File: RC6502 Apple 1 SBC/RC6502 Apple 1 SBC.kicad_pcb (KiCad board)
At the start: 2 copper layers, 99.1 x 99.7 mm, 48 parts, among them J1 VP GND, J10 RAM_EN, J11 PIA_EN, J2 Arduino Nano, J3 Backplane, J4 Hole, J5 Hole, J6 Hole, J7 Hole, J8 Power, J9 ROM_EN, SW1 RESET, U1 WD65C02, U2 HM62256BLP-7, U3 74HCT138, U4 28C256, U5 74HCT00, U6 NE555, U7 74HCT04, U8 WD65C21, U9 MCP23S17, X1 1MHz

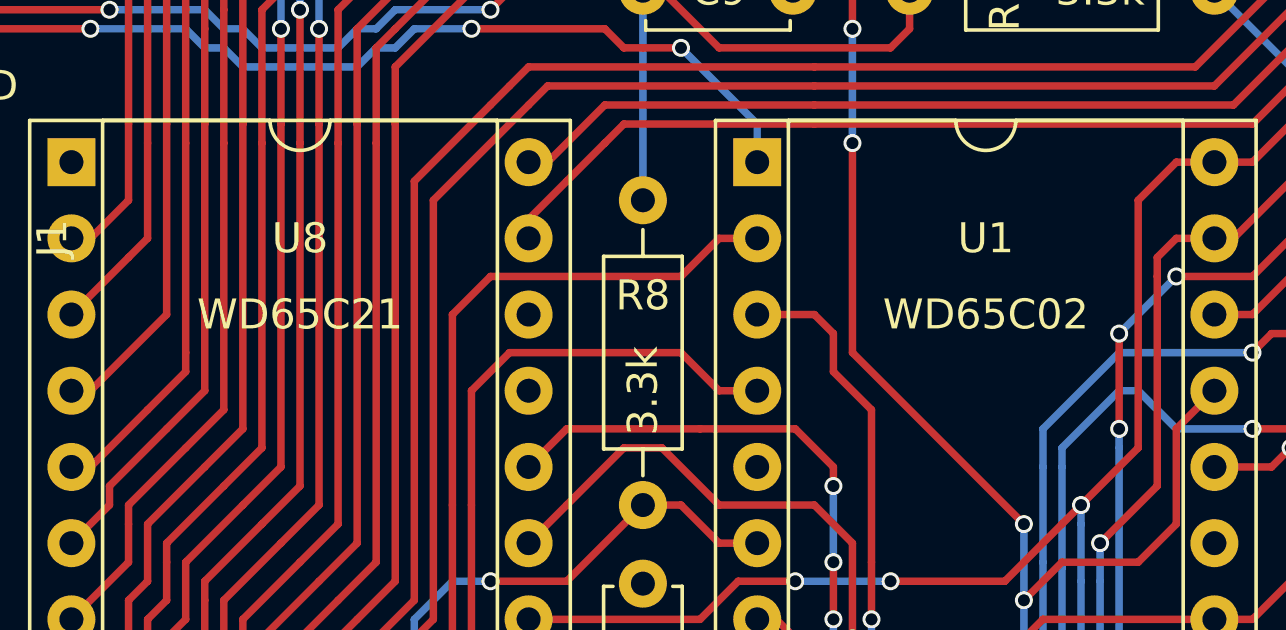
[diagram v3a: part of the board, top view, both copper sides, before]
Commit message: Cleaned up SBC schematic some more
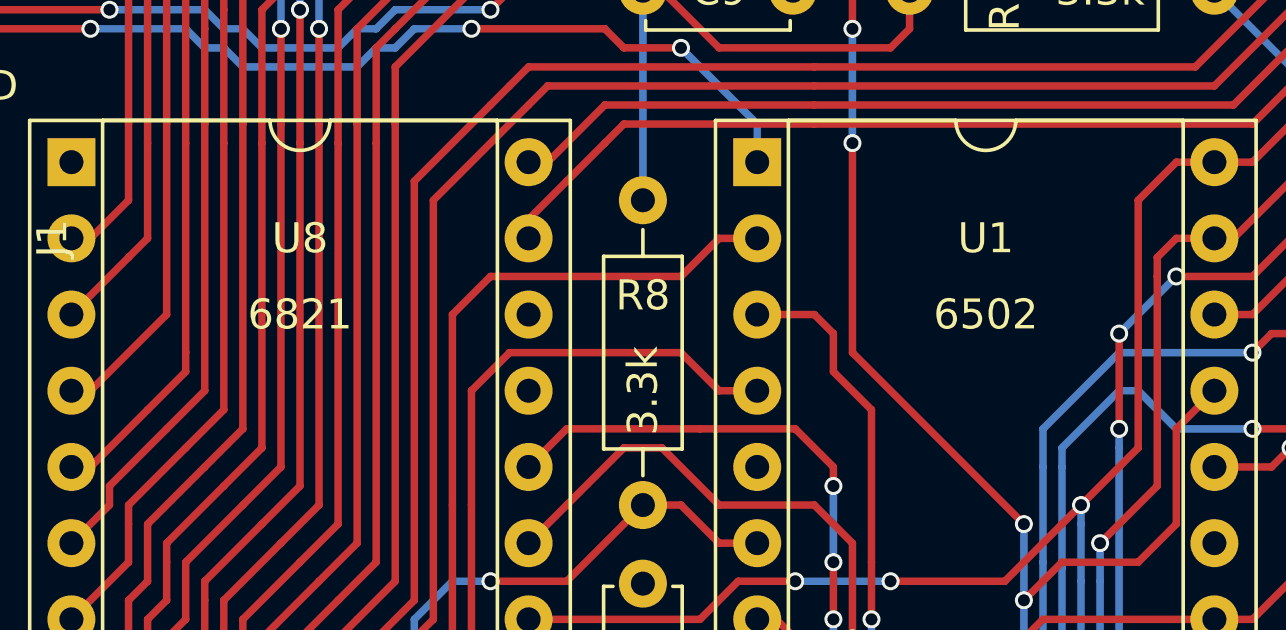
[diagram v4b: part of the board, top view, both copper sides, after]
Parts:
- U1: value WD65C02 -> 6502
- U8: value WD65C21 -> 6821
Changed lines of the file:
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@@
     (34 B.Paste user)
     (35 F.Paste user)
-    (36 B.SilkS user hide)
+    (36 B.SilkS user)
     (37 F.SilkS user)
     (38 B.Mask user)
@@
       (effects (font (size 1 1) (thickness 0.15)))
     )
-    (fp_text value WD65C02 (at 7.62 5.08 180) (layer F.SilkS)
+    (fp_text value 6502 (at 7.62 5.08 180) (layer F.SilkS)
       (effects (font (size 1 1) (thickness 0.15)))
     )
@@
       (effects (font (size 1 1) (thickness 0.15)))
     )
-    (fp_text value WD65C21 (at 7.62 5.08) (layer F.SilkS)
-      (effects (font (size 1 1) (thickness 0.15)))
-    )
+    (fp_text value 6821 (at 7.62 5.08) (layer F.SilkS)
+      (effects (font (size 1 1) (thickness 0.15)))
+    )

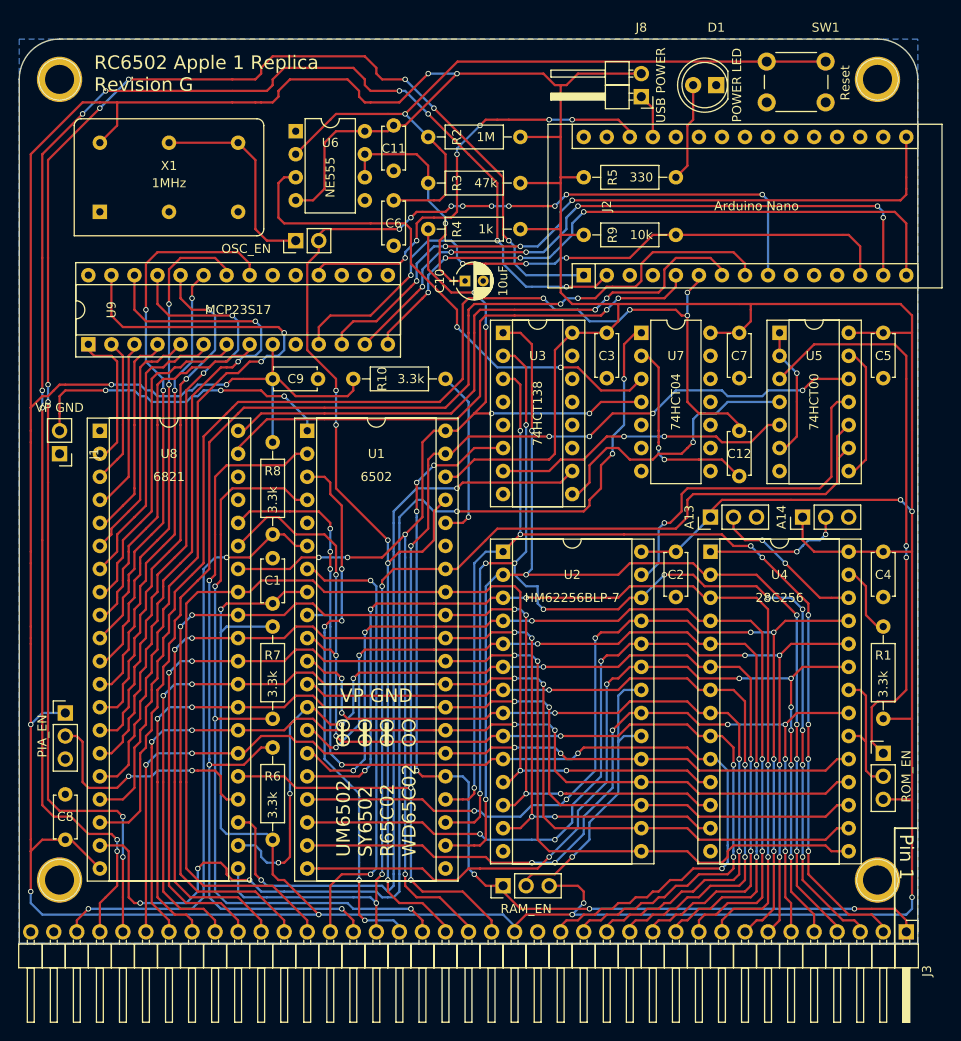
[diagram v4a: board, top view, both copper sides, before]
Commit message: Tweaked silkscreen
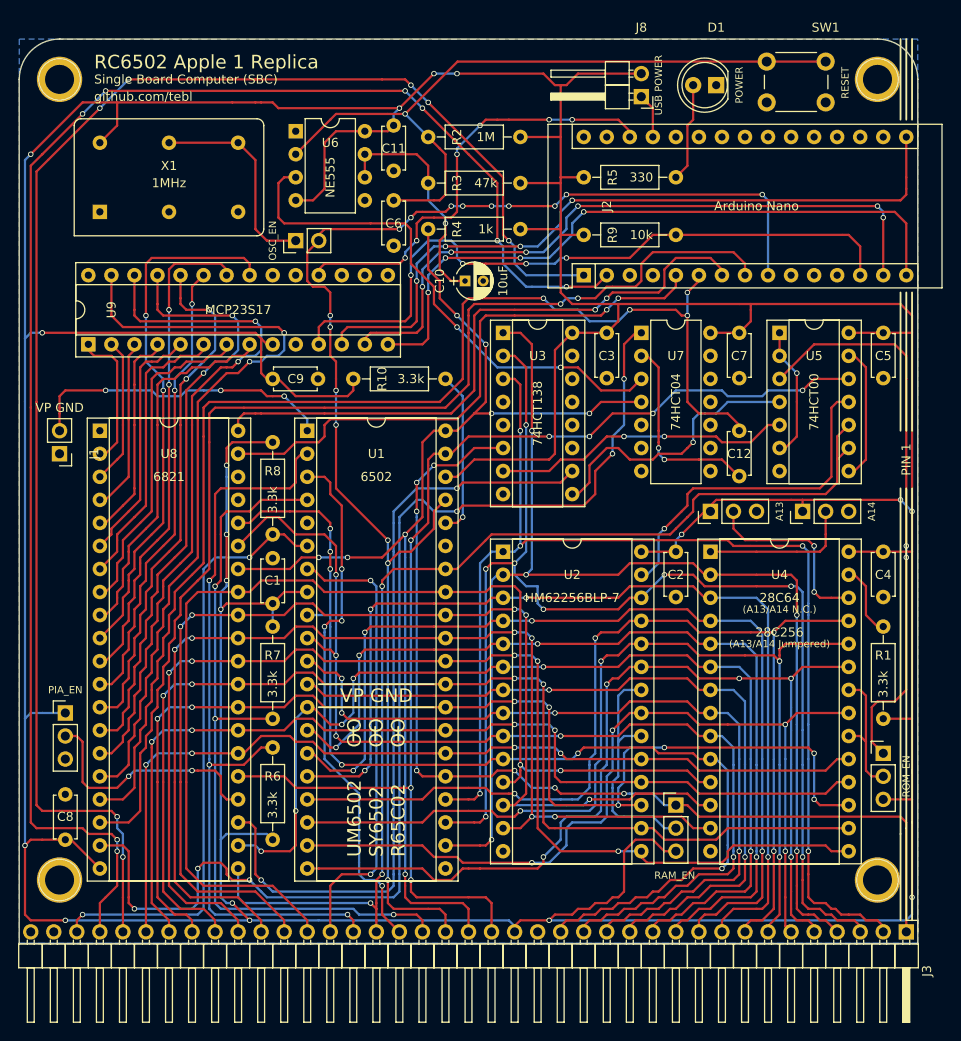
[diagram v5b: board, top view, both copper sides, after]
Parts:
- moved J10 21.0 mm to (188.6, 123.8), turned to 0 degrees
- moved A13 0.64 mm to (192.4, 91.4)
- moved A14 0.64 mm to (202.6, 91.4)
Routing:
- net VCC: track 668.5 -> 684.6 mm, vias 13 -> 18
- net D5: track 115.2 -> 128.3 mm, vias 4 -> 8
- net Net-(J10-Pad2): track 32.3 -> 26.3 mm, vias 1 -> 0
- net A14: track 129.9 -> 135.5 mm, vias 9 -> 5
- net A12: track 136.5 -> 140.2 mm, vias 7 -> 5
- net A13_W: track 17.1 -> 20.7 mm
- net D1: track 125.9 -> 129.0 mm, vias 6 -> 5
- net Net-(J2-Pad14): track 72.6 -> 75.5 mm
- net A13: track 138.4 -> 141.0 mm, vias 11 -> 8
- net A11: track 107.4 -> 110.0 mm, vias 8 -> 5
- net Net-(J2-Pad13): track 73.5 -> 76.1 mm
- net Net-(J2-Pad16): track 78.0 -> 80.6 mm
- net Net-(J2-Pad15): track 72.0 -> 74.3 mm
- net CLOCK: track 156.2 -> 158.3 mm, vias 14 -> 16
- net PHI2: track 129.3 -> 131.1 mm
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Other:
- board text added: "$0000 - $7FFF"
- board text added: "$D010 - $D012"
- board text added: "$E000 - $FFFF"
- board text added: "(A13/A14 Jumpered)"
- board text added: "(A13/A14 N.C.)"
- board text added: "0100.1FFF"
- board text added: "0100:FF"
- board text added: "6502 CPU"
- board text added: "6821 PIA"
- board text added: "ADDRESS DECODING"
- board text added: "ARDUINO I/O EXPANDER"
- board text added: "CHANGE MEMORY"
- board text added: "COMMAND"
- board text added: "DUMP MEMORY"
- board text added: "EEPROM"
- board text added: "HEX INVERTER"
- board text added: "Jumper to power SBC from Arduino, not recommended with expansions."
- board text added: "NAND GATES"
- board text added: "OO OO OO"
- board text added: "PIN 1"
- board text added: "POWER"
- board text added: "POWER-ON RESET"
- board text added: "PROGRAM"
- board text added: "RC6502 Apple 1 Replica"
- board text added: "RESET"
- board text added: "Revision H"
- board text added: "STATIC RAM"
- board text added: "SYSTEM CLOCK 1 MHZ TTL OSCILLATOR"
- board text added: "Single Board Computer (SBC)"
- board text added: "UM6502 SY6502 R65C02"
- board text added: "github.com/tebl"
- board text removed: "$0000-$1FFF $2000-$3FFF $4000-$5FFF $6000-$7FFF $0000-$1FFF"
- board text removed: "28C256"
- board text removed: "8K window"
- board text removed: "Address decoding"
- board text removed: "Arduino I/O Expander"
- board text removed: "Command"
- board text removed: "Dump user memory: 0100.1FFF Change $0100 to FF: 0100:FF"
- board text removed: "Jumper me when NOT using powered backplane"
- board text removed: "NAND Gate"
- board text removed: "OO OO OO OO"
- board text removed: "OOO OOO OOO OOO OOO"
- board text removed: "POWER LED"
- board text removed: "Power on reset"
- board text removed: "Program"
- board text removed: "RC6502 Apple 1 Replica Revision G"
- board text removed: "Reset"
- board text removed: "Signal inverter"
- board text removed: "System clock 1 Mhz oscillator"
- board text removed: "UM6502 SY6502 R65C02 WD65C02"
- board text removed: "https://hvetebolle.blogspot.com"

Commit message: SBC board cleaned up and exported
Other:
- board text removed: "Pin 1"
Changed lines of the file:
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@@
     (area 114.23 35.22 220.820001 148.420001)
     (thickness 1.6)
-    (drawings 200)
+    (drawings 197)
     (tracks 2389)
     (zones 0)
@@
     (35 F.Paste user hide)
     (36 B.SilkS user)
-    (37 F.SilkS user hide)
+    (37 F.SilkS user)
     (38 B.Mask user)
     (39 F.Mask user)
@@
     (effects (font (size 1.5 1.5) (thickness 0.2)) (justify left))
   )
-  (gr_text "Pin 1" (at 213.995 127 90) (layer B.SilkS)
-    (effects (font (size 1.5 1.5) (thickness 0.3)) (justify left mirror))
-  )
-  (gr_line (start 212.725 126.365) (end 212.725 133.985) (angle 90) (layer B.SilkS) (width 0.2))
-  (gr_line (start 215.265 126.365) (end 212.725 126.365) (angle 90) (layer B.SilkS) (width 0.2))
   (gr_line (start 182.88 42.545) (end 182.88 46.355) (angle 90) (layer B.SilkS) (width 0.2))
   (gr_line (start 158.75 46.99) (end 186.055 46.99) (angle 90) (layer B.SilkS) (width 0.2))
